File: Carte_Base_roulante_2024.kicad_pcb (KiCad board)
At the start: 2 copper layers, 63 parts, among them U1 STM32G484RETx

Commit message: compact : alim, encodeur, imu
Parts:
- added SWITCH1: SW_Push, ENAC_robotique:SWITCH_DTSM31NV, F.Cu at (164.1, 78.1)
- C1, C10, C11, C12, C13, C14, C15, C16, C17, C18, C19, C20, C21, C22, C3, C5, C7, C8, C9: footprint Capacitor_SMD:C_0805_2012Metric -> Capacitor_SMD:C_0603_1608Metric
- C23, C24: footprint Capacitor_SMD:C_1206_3216Metric -> Capacitor_SMD:C_0603_1608Metric
- MOT3: moved to B.Cu
- moved R1 62.6 mm to (232.4, 58.8), turned to -90 degrees
- moved C4 45.0 mm to (207.0, 93.4), turned to 180 degrees
- moved C22 38.8 mm to (140.9, 97.2), turned to 90 degrees
- moved LED1 38.1 mm to (247.9, 68.6)
- moved LED2 38.1 mm to (247.6, 65.9)
- moved R6 38.1 mm to (244.1, 65.9)
- moved R10 38.1 mm to (244.2, 68.6)
- moved C6 37.3 mm to (192.8, 101.6)
- moved C20 37.3 mm to (143.0, 97.2), turned to 90 degrees
- moved C21 36.2 mm to (145.0, 97.2), turned to 90 degrees
- moved C3 35.7 mm to (213.7, 96.9), turned to -90 degrees
- moved R5 35.0 mm to (148.6, 102.6), turned to -90 degrees
- moved D5 34.9 mm to (148.6, 106.0), turned to 90 degrees
- moved C19 33.4 mm to (148.6, 99.2), turned to 90 degrees
- moved U2 32.8 mm to (220.9, 95.2), turned to 0 degrees
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- renumbered LED_ALIM to D5, IMU to IMU1, ENC1 to J11, ENC2 to J4, ENC3 to J5, P-MOSFET to Q2, CS to TP_CS1, MISO to TP_MISO1, MOSI to TP_MOSI1, SCK to TP_SCK1, ZENER to ZENER1
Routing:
- net +3.3V: track 0.00 -> 49.0 mm
- net RST: track 0.00 -> 29.4 mm
- net Enc3_A: track 0.00 -> 23.4 mm, vias 0 -> 2
- net Enc3_B: track 0.00 -> 21.2 mm
- net Enc2_A: track 0.00 -> 14.4 mm
- net Enc2_B: track 0.00 -> 12.1 mm
- net SWCLK: track 0.00 -> 11.8 mm
- net SWDIO: track 0.00 -> 11.3 mm
- net Enc1_A: track 0.00 -> 10.6 mm
- net SPI1_CS_IMU: track 0.00 -> 8.68 mm, vias 0 -> 2
- net SPI1_SCK: track 0.00 -> 7.95 mm, vias 0 -> 2
- net UART4_TX: track 0.00 -> 7.37 mm
- net Enc1_B: track 0.00 -> 7.19 mm
- net /BOOT 0: track 0.00 -> 7.10 mm
- net +BATT: track 0.00 -> 6.70 mm
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- added copper zone on F.Cu, net +5V
- added copper zone on F.Cu, net +BATT
- added copper zone on F.Cu, net Net-(ALIM1-Pin_2)
- added copper zone on F.Cu, net Net-(MOT1-Pin_1)
- added copper zone on F.Cu, net Net-(MOT1-Pin_2)
- added copper zone on F.Cu, net Net-(MOT2-Pin_1)
- added copper zone on F.Cu, net Net-(MOT2-Pin_2)
- added copper zone on F.Cu, net Net-(MOT3-Pin_1)
- added copper zone on F.Cu, net Net-(MOT3-Pin_2)

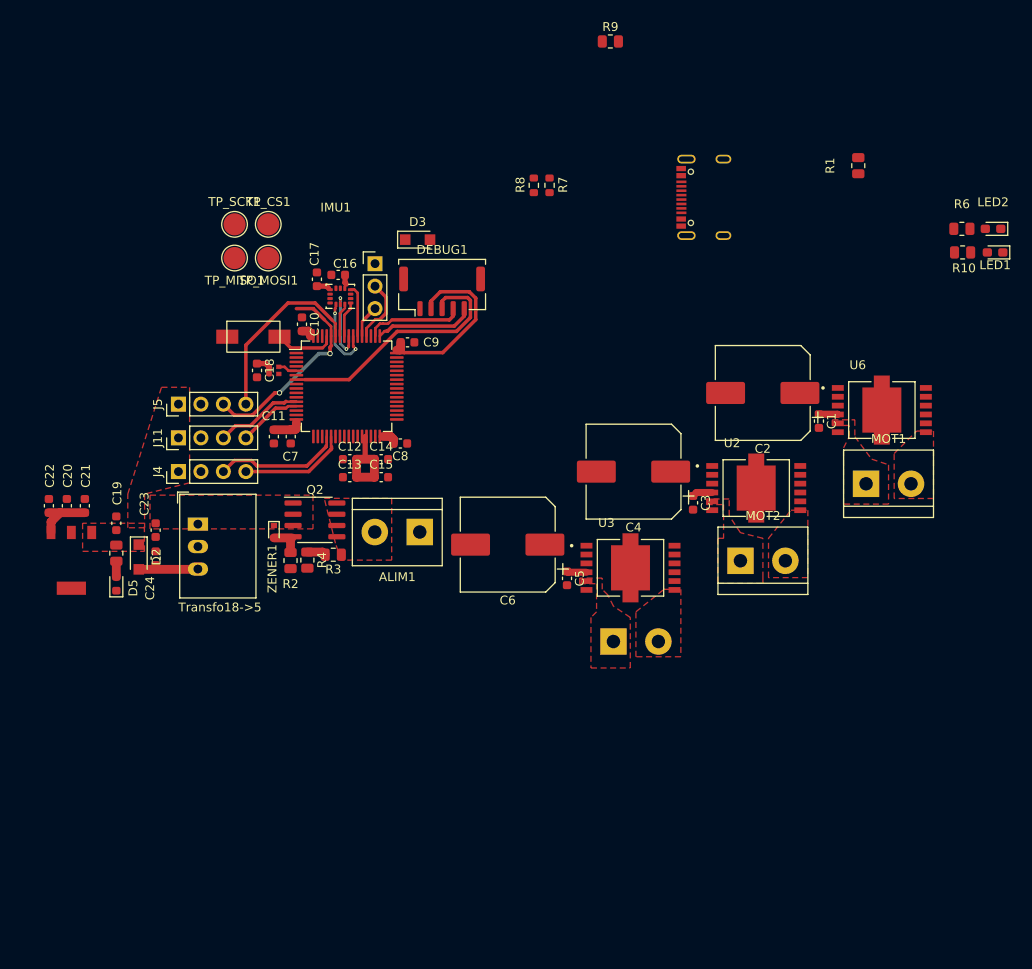
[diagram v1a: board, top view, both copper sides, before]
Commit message: placement amélioré
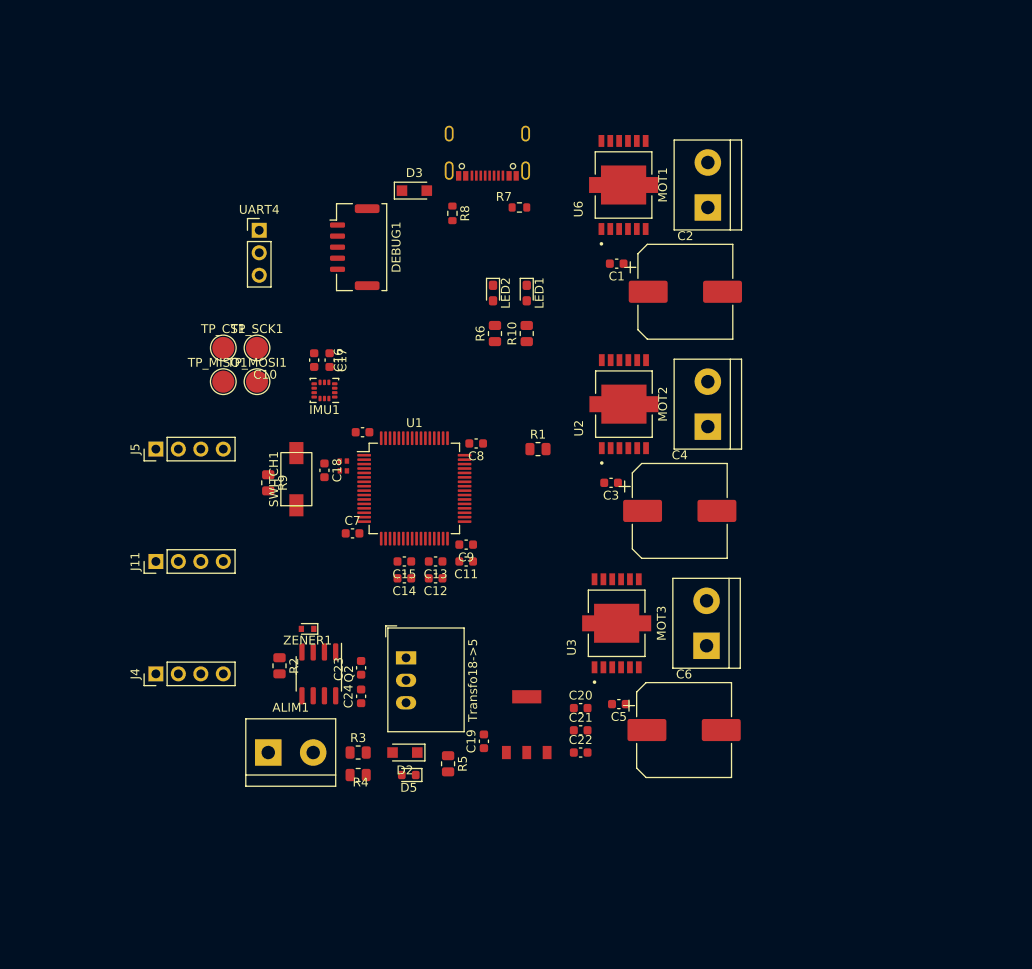
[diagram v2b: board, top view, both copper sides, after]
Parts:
- J11: value ENC1 -> ENCA
- J4: value ENC2 -> ENCB
- J5: value ENC3 -> ENCC
- MOT3: moved to F.Cu
- moved C22 66.2 mm to (201.0, 125.1), turned to 0 degrees
- moved R9 63.1 mm to (165.7, 94.6), turned to -90 degrees
- moved C20 62.4 mm to (201.0, 120.1), turned to 0 degrees
- moved C21 61.5 mm to (201.0, 122.6), turned to 0 degrees
- moved LED2 57.0 mm to (191.1, 73.2), turned to -90 degrees
- moved Transfo5->3.3 54.7 mm to (194.9, 121.9), turned to 90 degrees
- moved R6 54.1 mm to (191.4, 77.7), turned to 90 degrees
- moved LED1 53.1 mm to (194.9, 73.2), turned to -90 degrees
- moved R10 50.1 mm to (194.9, 77.7), turned to 90 degrees
- moved R1 48.3 mm to (196.2, 90.8), turned to 0 degrees
- moved C19 48.3 mm to (190.1, 123.8)
- moved R5 44.4 mm to (186.1, 126.4)
- moved D5 39.5 mm to (181.6, 127.6), turned to 180 degrees
- moved U6 38.7 mm to (205.9, 61.0), turned to 90 degrees
- moved D2 37.3 mm to (181.2, 125.1), turned to 180 degrees
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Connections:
- U1 pad 33: DIR2 -> DIR3
- U1 pad 34: DIR1 -> DIR2
- U1 pad 35: PWM1 -> PWM3
- U1 pad 37: PWM3 -> PWM1
- U1 pad 38: DIR3 -> DIR1
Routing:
- net +3.3V: track 49.0 -> 0.00 mm
- net RST: track 29.4 -> 0.00 mm
- net Enc3_A: track 23.4 -> 0.00 mm, vias 2 -> 0
- net Enc3_B: track 21.2 -> 0.00 mm
- net Enc2_A: track 14.4 -> 0.00 mm
- net Enc2_B: track 12.1 -> 0.00 mm
- net SWCLK: track 11.8 -> 0.00 mm
- net SWDIO: track 11.3 -> 0.00 mm
- net Enc1_A: track 10.6 -> 0.00 mm
- net SPI1_CS_IMU: track 8.68 -> 0.00 mm, vias 2 -> 0
- net SPI1_SCK: track 7.95 -> 0.00 mm, vias 2 -> 0
- net UART4_TX: track 7.37 -> 0.00 mm
- net Enc1_B: track 7.19 -> 0.00 mm
- net /BOOT 0: track 7.10 -> 0.00 mm
- net +BATT: track 6.70 -> 0.00 mm
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- removed copper zone on F.Cu, net +5V
- removed copper zone on F.Cu, net +BATT
- removed copper zone on F.Cu, net Net-(ALIM1-Pin_2)
- removed copper zone on F.Cu, net Net-(MOT1-Pin_1)
- removed copper zone on F.Cu, net Net-(MOT1-Pin_2)
- removed copper zone on F.Cu, net Net-(MOT2-Pin_1)
- removed copper zone on F.Cu, net Net-(MOT2-Pin_2)
- removed copper zone on F.Cu, net Net-(MOT3-Pin_1)
- removed copper zone on F.Cu, net Net-(MOT3-Pin_2)

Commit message: j'essaie
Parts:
- moved C14 0.17 mm to (181.2, 105.5)
- moved C15 0.17 mm to (181.2, 103.6)
- moved C12 0.17 mm to (184.8, 105.5)
- moved C13 0.17 mm to (184.8, 103.6)
- turned D5 to 0 degrees
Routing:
- net +3.3V: track 0.00 -> 30.2 mm
- net Enc2_A: track 0.00 -> 28.7 mm
- net Enc2_B: track 0.00 -> 27.8 mm
- net Enc1_A: track 0.00 -> 21.2 mm
- net Enc1_B: track 0.00 -> 18.1 mm
- net /BOOT 0: track 0.00 -> 16.5 mm
- net +5V: track 0.00 -> 5.61 mm, vias 0 -> 1
- net OSCILATEUR: track 0.00 -> 2.04 mm
- added copper zone on F.Cu, net +3.3V
- added copper zone on B.Cu, net +5V
- added copper zone on F.Cu, net +5V
- added copper zone on F.Cu, net +BATT
- added copper zone on F.Cu, net Net-(ALIM1-Pin_2)
- added copper zone on F.Cu, net Net-(D2-A)
- added copper zone on F.Cu, net Net-(D5-A)
- added copper zone on F.Cu, net Net-(MOT3-Pin_1)
- added copper zone on F.Cu, net Net-(Q2-G)

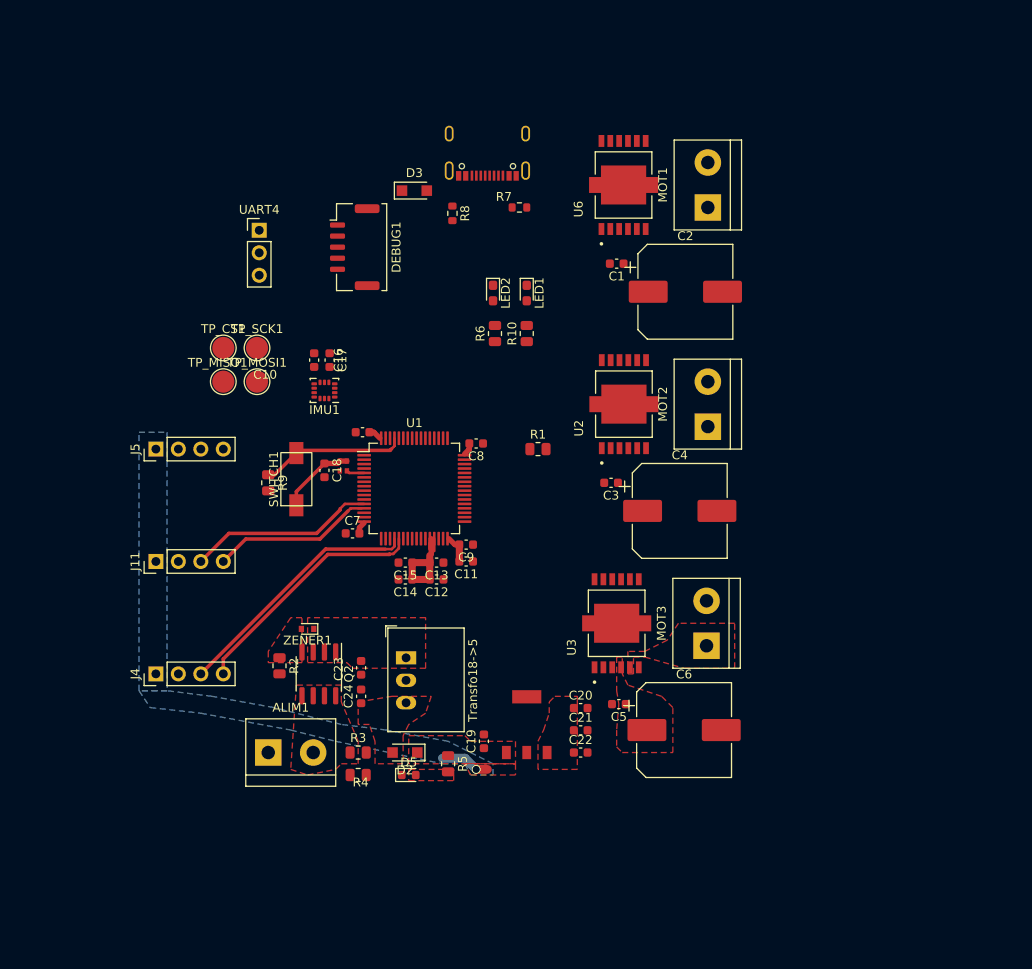
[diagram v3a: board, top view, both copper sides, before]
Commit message: changement alim et plan BATT
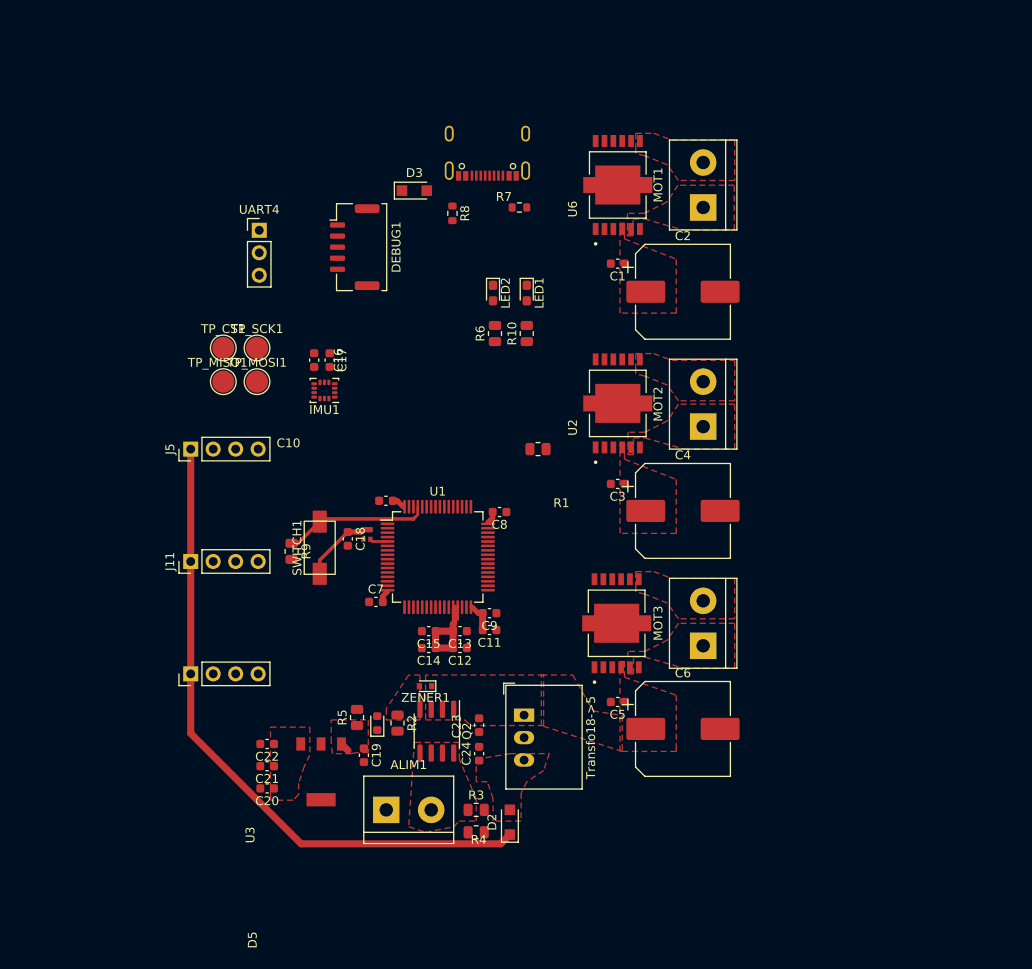
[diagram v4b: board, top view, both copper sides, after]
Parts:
- moved C20 36.6 mm to (165.6, 129.1), turned to 180 degrees
- moved C21 35.7 mm to (165.6, 126.6), turned to 180 degrees
- moved C22 35.4 mm to (165.6, 124.1), turned to 180 degrees
- moved Transfo5->3.3 23.8 mm to (171.7, 127.3), turned to -90 degrees
- moved C23 14.8 mm to (189.6, 122.0)
- moved Q2 14.8 mm to (184.8, 122.7)
- moved Transfo18->5 14.8 mm to (194.6, 120.9)
- moved C24 14.8 mm to (189.6, 125.2)
- moved R2 14.8 mm to (180.3, 121.8)
- moved ALIM1 14.8 mm to (179.1, 131.6)
- moved R3 14.8 mm to (189.2, 131.6)
- moved ZENER1 14.8 mm to (183.5, 117.6)
- moved R4 14.8 mm to (189.2, 134.1)
- moved D2 14.2 mm to (193.0, 133.0), turned to 90 degrees
- moved C19 13.7 mm to (176.5, 125.4), turned to -90 degrees
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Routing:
- net +5V: track 5.61 -> 74.9 mm, vias 1 -> 0
- net Enc2_A: track 28.7 -> 0.00 mm
- net Enc2_B: track 27.8 -> 0.00 mm
- net Enc1_A: track 21.2 -> 0.00 mm
- net Enc1_B: track 18.1 -> 0.00 mm
- added copper zone on F.Cu, net Net-(MOT1-Pin_1)
- added copper zone on F.Cu, net Net-(MOT1-Pin_2)
- added copper zone on F.Cu, net Net-(MOT2-Pin_1)
- added copper zone on F.Cu, net Net-(MOT2-Pin_2)
- added copper zone on F.Cu, net Net-(MOT3-Pin_2)
- removed copper zone on B.Cu, net +5V
- removed copper zone on F.Cu, net Net-(D5-A)

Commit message: + batt ok ?
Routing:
- net +3.3V: track 30.2 -> 101.7 mm
- net +5V: track 74.9 -> 85.5 mm
- net +BATT: vias 0 -> 6
- added copper zone on B.Cu, net +BATT
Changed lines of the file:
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@@
     )
   )
+  (via (at 208.026 119.38) (size 1) (drill 0.8) (layers "F.Cu" "B.Cu") (free) (net 1))
+  (via (at 211.074 94.996) (size 1) (drill 0.8) (layers "F.Cu" "B.Cu") (free) (net 1))
+  (via (at 211.328 124.46) (size 1) (drill 0.8) (layers "F.Cu" "B.Cu") (free) (net 1))
+  (via (at 211.328 99.822) (size 1) (drill 0.8) (layers "F.Cu" "B.Cu") (free) (net 1))
+  (via (at 208.534 94.234) (size 1) (drill 0.8) (layers "F.Cu" "B.Cu") (free) (net 1))
+  (via (at 211.074 119.634) (size 1) (drill 0.8) (layers "F.Cu" "B.Cu") (free) (net 1))
+  (segment (start 186.786 108.204) (end 186.786 107.931748) (width 0.6) (layer "F.Cu") (net 3))
+  (segment (start 169.404 121.172) (end 178.676 111.9) (width 0.6) (layer "F.Cu") (net 3))
+  (segment (start 188.677 107.397) (end 188.786 107.506) (width 0.6) (layer "F.Cu") (net 3))
   (segment (start 189.966 109.347) (end 189.966 111.252) (width 0.8) (layer "F.Cu") (net 3))
   (segment (start 174.726 100.177) (end 176.196 100.177) (width 0.6) (layer "F.Cu") (net 3))
   (segment (start 191.096 97.917) (end 191.096 98.562) (width 0.6) (layer "F.Cu") (net 3))
+  (segment (start 203.605 116.435) (end 203.605 115.465) (width 0.8) (layer "F.Cu") (net 3))
   (segment (start 186.625 113.284) (end 186.625 111.379) (width 0.8) (layer "F.Cu") (net 3))
+  (segment (start 186.625 113.284) (end 186.625 113.759) (width 0.8) (layer "F.Cu") (net 3))
   (segment (start 186.636 108.672) (end 186.636 109.883) (width 0.3) (layer "F.Cu") (net 3))
   (segment (start 180.311 96.647) (end 180.986 97.322) (width 0.6) (layer "F.Cu") (net 3))
   (segment (start 177.266 99.907) (end 176.466 99.907) (width 0.6) (layer "F.Cu") (net 3))
   (segment (start 187.136 108.672) (end 187.136 110.073) (width 0.3) (layer "F.Cu") (net 3))
+  (segment (start 186.786 110.423) (end 186.786 108.204) (width 0.6) (layer "F.Cu") (net 3))
+  (segment (start 179.211 106.897) (end 178.676 107.432) (width 0.6) (layer "F.Cu") (net 3))
+  (segment (start 187.320748 101.397) (end 187.320748 107.397) (width 0.6) (layer "F.Cu") (net 3))
   (segment (start 171.551 103.352) (end 174.726 100.177) (width 0.4) (layer "F.Cu") (net 3))
+  (segment (start 186.786 107.731748) (end 185.951252 106.897) (width 0.6) (layer "F.Cu") (net 3))
+  (segment (start 186.625 110.584) (end 186.786 110.423) (width 0.6) (layer "F.Cu") (net 3))
+  (segment (start 186.625 113.759) (end 189.606 116.74) (width 0.8) (layer "F.Cu") (net 3))
   (segment (start 184.645 113.284) (end 186.625 113.284) (width 0.8) (layer "F.Cu") (net 3))
+  (segment (start 189.620748 99.097) (end 187.320748 101.397) (width 0.6) (layer "F.Cu") (net 3))
+  (segment (start 186.786 108.204) (end 186.786 107.731748) (width 0.6) (layer "F.Cu") (net 3))
   (segment (start 179.806 96.647) (end 180.311 96.647) (width 0.6) (layer "F.Cu") (net 3))
+  (segment (start 185.951252 106.897) (end 179.211 106.897) (width 0.6) (layer "F.Cu") (net 3))
   (segment (start 176.196 100.177) (end 176.466 99.907) (width 0.6) (layer "F.Cu") (net 3))
+  (segment (start 186.786 107.931748) (end 187.320748 107.397) (width 0.6) (layer "F.Cu") (net 3))
   (segment (start 186.625 111.379) (end 186.625 110.584) (width 0.8) (layer "F.Cu") (net 3))
+  (segment (start 188.786 107.506) (end 188.786 108.672) (width 0.6) (layer "F.Cu") (net 3))
+  (segment (start 203.3 116.74) (end 203.605 116.435) (width 0.8) (layer "F.Cu") (net 3))
   (segment (start 191.096 98.562) (end 190.561 99.097) (width 0.6) (layer "F.Cu") (net 3))
-  (segment (start 186.786 110.423) (end 186.786 108.672) (width 0.6) (layer "F.Cu") (net 3))
+  (segment (start 187.320748 107.397) (end 188.677 107.397) (width 0.6) (layer "F.Cu") (net 3))
+  (segment (start 175.501 104.902) (end 171.551 104.902) (width 0.6) (layer "F.Cu") (net 3))
+  (segment (start 189.606 116.74) (end 203.3 116.74) (width 0.8) (layer "F.Cu") (net 3))
   (segment (start 189.966 109.347) (end 189.461 109.347) (width 0.6) (layer "F.Cu") (net 3))
   (segment (start 184.645 113.284) (end 184.645 111.379) (width 0.8) (layer "F.Cu") (net 3))
+  (segment (start 190.561 99.097) (end 189.620748 99.097) (width 0.6) (layer "F.Cu") (net 3))
+  (segment (start 169.404 124.129) (end 169.404 121.172) (width 0.6) (layer "F.Cu") (net 3))
   (segment (start 189.461 109.347) (end 188.786 108.672) (width 0.6) (layer "F.Cu") (net 3))
-  (segment (start 178.676 107.432) (end 179.211 106.897) (width 0.6) (layer "F.Cu") (net 3))
+  (segment (start 178.676 108.077) (end 175.501 104.902) (width 0.6) (layer "F.Cu") (net 3))
   (segment (start 171.551 104.902) (end 171.551 103.352) (width 0.4) (layer "F.Cu") (net 3))
   (segment (start 186.636 109.172) (end 186.636 109.883) (width 0.3) (layer "F.Cu") (net 3))
+  (segment (start 178.676 111.9) (end 178.676 107.432) (width 0.6) (layer "F.Cu") (net 3))
   (segment (start 178.676 108.077) (end 178.676 107.432) (width 0.6) (layer "F.Cu") (net 3))
-  (segment (start 186.625 110.584) (end 186.786 110.423) (width 0.6) (layer "F.Cu") (net 3))
   (segment (start 184.645 111.379) (end 186.625 111.379) (width 0.8) (layer "F.Cu") (net 3))
+  (segment (start 191.994 135.412) (end 175.006 135.412) (width 0.8) (layer "F.Cu") (net 4))
   (segment (start 193.04 134.366) (end 191.994 135.412) (width 0.8) (layer "F.Cu") (net 4))
-  (segment (start 174.752 124.877) (end 174.004 124.129) (width 0.8) (layer "F.Cu") (net 4))
-  (segment (start 191.994 135.412) (end 169.44904 135.412) (width 0.8) (layer "F.Cu") (net 4))
   (segment (start 156.972 103.505) (end 156.972 116.205) (width 0.8) (layer "F.Cu") (net 4))
   (segment (start 169.44904 135.412) (end 156.972 122.93496) (width 0.8) (layer "F.Cu") (net 4))
+  (segment (start 175.006 125.131) (end 174.004 124.129) (width 0.8) (layer "F.Cu") (net 4))
+  (segment (start 175.006 135.412) (end 169.44904 135.412) (width 0.8) (layer "F.Cu") (net 4))
+  (segment (start 175.006 135.412) (end 175.006 125.131) (width 0.8) (layer "F.Cu") (net 4))
   (segment (start 156.972 122.93496) (end 156.972 116.205) (width 0.8) (layer "F.Cu") (net 4))
   (segment (start 156.972 90.805) (end 156.972 103.505) (width 0.8) (layer "F.Cu") (net 4))
@@
     (polygon
       (pts
-        (xy 211.836 124.968)
-        (xy 205.486 124.968)
+        (xy 212.09 125.476)
+        (xy 205.486 125.476)
         (xy 205.486 114.808)
         (xy 205.994 114.808)
         (xy 205.994 116.586)
-        (xy 211.836 118.618)
-        (xy 211.836 124.714)
+        (xy 212.09 118.872)
+        (xy 212.09 124.968)
       )
     )
@@
         (xy 188.595 122.047)
         (xy 196.85 122.047)
-        (xy 196.85 116.332)
+        (xy 196.85 119.126)
       )
     )
@@
     (polygon
       (pts
-        (xy 211.836 100.33)
-        (xy 205.486 100.33)
+        (xy 212.09 100.838)
+        (xy 205.486 100.838)
         (xy 205.486 90.17)
         (xy 205.994 90.17)
         (xy 205.994 91.948)
-        (xy 211.836 94.234)
-        (xy 211.836 100.076)
+        (xy 212.09 94.234)
+        (xy 212.09 100.076)
       )
     )
@@
         (xy 205.74 124.968)
         (xy 196.596 122.047)
-        (xy 196.596 116.332)
-        (xy 200.152 116.332)
+        (xy 196.596 119.126)
+        (xy 200.152 119.126)
         (xy 202.438 120.396)
         (xy 205.74 120.904)
@@
       )
     )
+  )
+  (zone (net 1) (net_name "+BATT") (layer "B.Cu") (hatch edge 0.5)
+    (priority 6)
+    (connect_pads (clearance 0.5))
+    (min_thickness 0.25) (filled_areas_thickness no)
+    (fill yes (thermal_gap 0.5) (thermal_bridge_width 0.5))
+    (polygon
+      (pts
+        (xy 212.344 125.73)
+        (xy 212.344 67.564)
+        (xy 205.232 67.564)
+        (xy 205.486 125.73)
+      )
+    )
